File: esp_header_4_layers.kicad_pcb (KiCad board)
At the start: 4 copper layers, 27.7 x 63.5 mm, 29 parts, among them J10 BM05B-SRSS, J11 BM05B-SRSS, J12 BM05B-SRSS, J2 JST_VH_B2P, J6 BM02B-SRSS-TB, J7 B3B-EH-A, J8 B3B-EH-A, J9 B3B-EH-A, Q1 AOD472A, SW1 SW_DIP_x01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

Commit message: untracked unnecessary files
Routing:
- net /In_6V: vias 22 -> 12
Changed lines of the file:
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@@
 	(layers
 		(0 "F.Cu" signal)
-		(4 "In1.Cu" signal)
-		(6 "In2.Cu" signal)
+		(4 "In1.Cu" power "GND.Cu")
+		(6 "In2.Cu" power "POWER.Cu")
 		(2 "B.Cu" signal)
 		(9 "F.Adhes" user "F.Adhesive")
@@
 		(capping no)
 		(filling no)
+		(zone_defaults)
 		(pcbplotparams
 			(layerselection 0x00000000_00000000_55555555_5755f5ff)
@@
 	)
 	(via
-		(at 116.2 45.5)
+		(at 110 47.5)
 		(size 0.6)
 		(drill 0.3)
@@
 	)
 	(via
-		(at 114.1 45.5)
+		(at 115 42.5)
 		(size 0.6)
 		(drill 0.3)
@@
 	)
 	(via
-		(at 113.3725 50.1)
-		(size 0.6)
-		(drill 0.3)
-		(layers "F.Cu" "B.Cu")
-		(net "/In_6V")
-	)
-	(via
-		(at 112 45.5)
-		(size 0.6)
-		(drill 0.3)
-		(layers "F.Cu" "B.Cu")
-		(free yes)
-		(net "/In_6V")
-	)
-	(via
-		(at 113.4 46.2)
-		(size 0.6)
-		(drill 0.3)
-		(layers "F.Cu" "B.Cu")
-		(free yes)
-		(net "/In_6V")
-	)
-	(via
-		(at 115.5 45.5)
-		(size 0.6)
-		(drill 0.3)
-		(layers "F.Cu" "B.Cu")
-		(free yes)
-		(net "/In_6V")
-	)
-	(via
-		(at 112 46.2)
-		(size 0.6)
-		(drill 0.3)
-		(layers "F.Cu" "B.Cu")
-		(free yes)
-		(net "/In_6V")
-	)
-	(via
-		(at 112.7 45.5)
-		(size 0.6)
-		(drill 0.3)
-		(layers "F.Cu" "B.Cu")
-		(free yes)
-		(net "/In_6V")
-	)
-	(via
-		(at 111.3 46.2)
-		(size 0.6)
-		(drill 0.3)
-		(layers "F.Cu" "B.Cu")
-		(free yes)
-		(net "/In_6V")
-	)
-	(via
-		(at 114.8 46.2)
-		(size 0.6)
-		(drill 0.3)
-		(layers "F.Cu" "B.Cu")
-		(free yes)
-		(net "/In_6V")
-	)
-	(via
-		(at 116.9 46.2)
+		(at 114.846513 47.534131)
 		(size 0.6)
 		(drill 0.3)
@@
 	)
 	(via
-		(at 114.8 45.5)
+		(at 112.5 42.5)
 		(size 0.6)
 		(drill 0.3)
@@
 	)
 	(via
-		(at 116.2 46.2)
+		(at 112.5 47.5)
 		(size 0.6)
 		(drill 0.3)
@@
 	)
 	(via
-		(at 117.6 46.2)
+		(at 117.5 42.5)
 		(size 0.6)
 		(drill 0.3)
@@
 	)
 	(via
-		(at 116.9 45.5)
+		(at 110 45.1)
 		(size 0.6)
 		(drill 0.3)
@@
 	)
 	(via
-		(at 111.3 45.5)
+		(at 115 45)
 		(size 0.6)
 		(drill 0.3)
@@
 	)
 	(via
-		(at 117.6 45.5)
+		(at 112.5 45)
 		(size 0.6)
 		(drill 0.3)
@@
 	)
 	(via
-		(at 113.4 45.5)
+		(at 110 42.5)
 		(size 0.6)
 		(drill 0.3)
@@
 	)
 	(via
-		(at 115.5 46.2)
+		(at 112.5 47.5)
 		(size 0.6)
 		(drill 0.3)
@@
 	)
 	(via
-		(at 113.3725 50.1)
-		(size 0.6)
-		(drill 0.3)
-		(layers "F.Cu" "B.Cu")
-		(net "/In_6V")
-	)
-	(via
-		(at 112.7 46.2)
-		(size 0.6)
-		(drill 0.3)
-		(layers "F.Cu" "B.Cu")
-		(free yes)
-		(net "/In_6V")
-	)
-	(via
-		(at 114.1 46.2)
+		(at 117.5 47.5)
 		(size 0.6)
 		(drill 0.3)
@@
 		(start 115.6525 54.3475)
 		(end 115.6525 56.4)
-		(width 0.4)
+		(width 1)
 		(layer "F.Cu")
 		(net "+6V")
@@
 	)
 	(segment
-		(start 112.9 67.3)
-		(end 112.95 67.25)
+		(start 112.95 67.25)
+		(end 112.95 65.592648)
 		(width 0.2)
 		(layer "F.Cu")
@@
 	)
 	(segment
-		(start 112.95 67.25)
-		(end 112.95 65.592648)
+		(start 113.280647 65.262001)
+		(end 114.046 65.262001)
 		(width 0.2)
 		(layer "F.Cu")
@@
 	)
 	(segment
-		(start 112.95 65.592648)
-		(end 113.280647 65.262001)
+		(start 112.9 67.3)
+		(end 112.95 67.25)
 		(width 0.2)
 		(layer "F.Cu")
@@
 	)
 	(segment
-		(start 113.280647 65.262001)
-		(end 114.046 65.262001)
+		(start 112.95 65.592648)
+		(end 113.280647 65.262001)
 		(width 0.2)
 		(layer "F.Cu")
@@
 	)
 	(segment
-		(start 112.9 67.3)
-		(end 112.1 67.3)
+		(start 112.1 67.3)
+		(end 112.08 67.32)
 		(width 0.2)
 		(layer "B.Cu")
@@
 	)
 	(segment
-		(start 112.08 67.32)
-		(end 108.05 67.32)
+		(start 112.9 67.3)
+		(end 112.1 67.3)
 		(width 0.2)
 		(layer "B.Cu")
@@
 	)
 	(segment
-		(start 112.1 67.3)
-		(end 112.08 67.32)
+		(start 112.08 67.32)
+		(end 108.05 67.32)
 		(width 0.2)
 		(layer "B.Cu")
@@
 		(polygon
 			(pts
-				(xy 110.05139 41.519538) (xy 120.75 41.4) (xy 122.200678 42.539819) (xy 122.16867 48.435121) (xy 109.741912 48.3785)
-				(xy 109.741901 48.3785) (xy 110.051374 41.519538)
+				(xy 110 41.519538) (xy 120.75 41.4) (xy 122.200678 42.539819) (xy 122.16867 48.435121) (xy 109.741912 48.3785)
+				(xy 109.741901 48.3785) (xy 109.724906 41.52022)
 			)
 		)

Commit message: made schematic clearer
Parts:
- C2: value 10uF@12V -> 47uF@10V
- D6: value LED BLUE -> LED YELLOW
- D7: value LED Green -> LED Yellow
- Q1: value AOD472A -> MS50N06

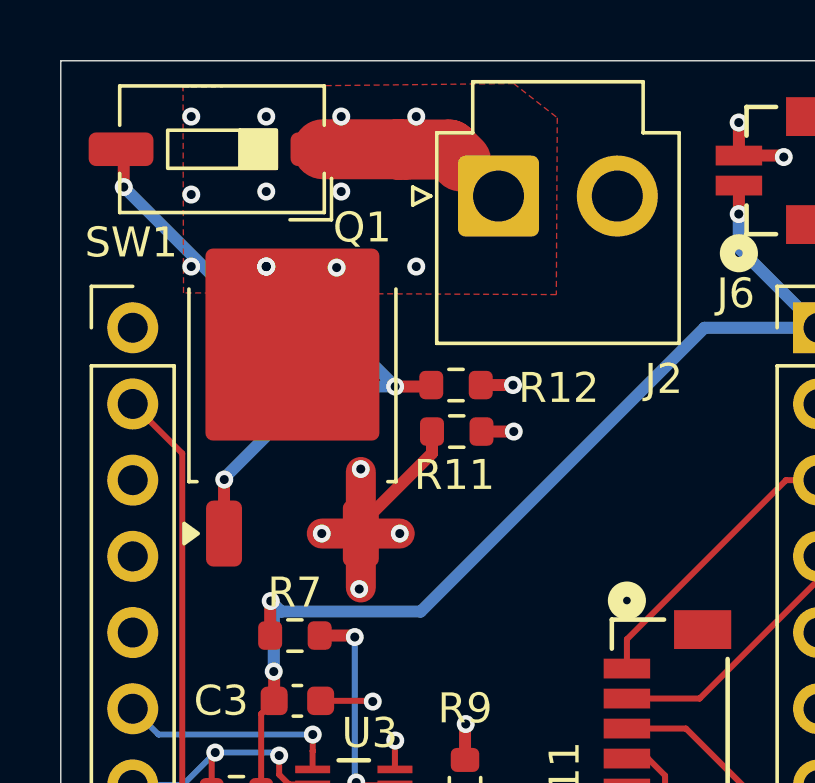
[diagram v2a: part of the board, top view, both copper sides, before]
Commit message: changed to PMOS instead of NMOS
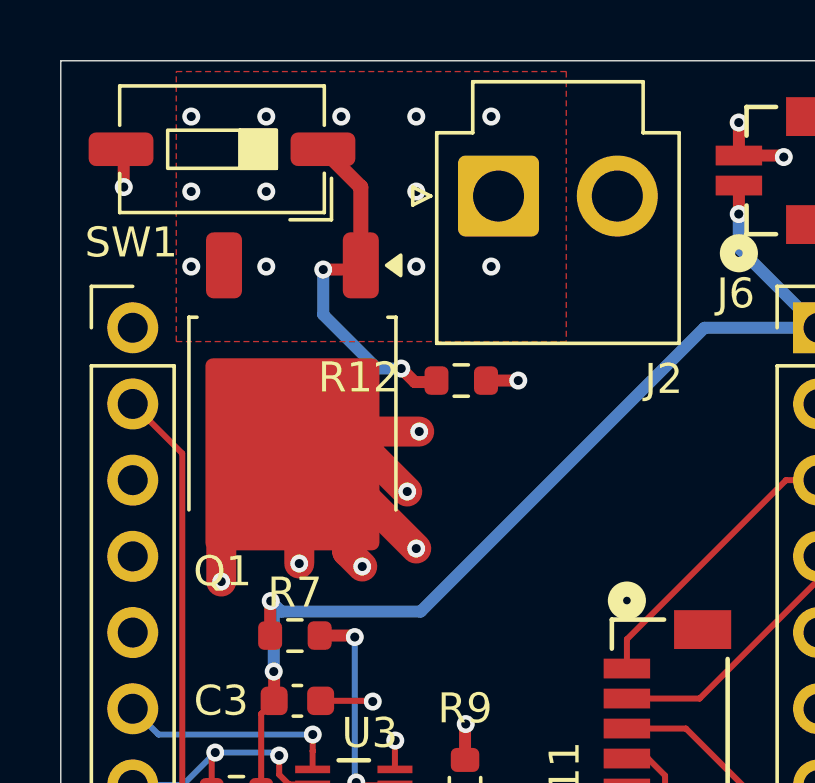
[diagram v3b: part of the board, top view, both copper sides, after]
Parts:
- removed R11: 100k, Resistor_SMD:R_0603_1608Metric
- moved Q1 1.14 mm to (113.4, 52.5), turned to -90 degrees
- moved R12 0.23 mm to (119.0, 51.3), turned to 180 degrees
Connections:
- Q1 pad D: /In_6V -> +6V
- Q1 pad S: +6V -> /In_6V
- R12 pad 1: /gate -> /In_6V
- R12 pad 2: GND -> /gate
- SW1 pad 1: /In_6V -> /gate
- SW1 pad 2: /gate -> GND
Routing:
- net +6V: track 15.2 -> 31.9 mm, vias 7 -> 9
- net /gate: track 23.0 -> 11.9 mm, vias 3 -> 2
- net /In_6V: track 4.78 -> 1.08 mm, vias 12 -> 13
- net GND: track 16.3 -> 15.4 mm, vias 13 -> 12

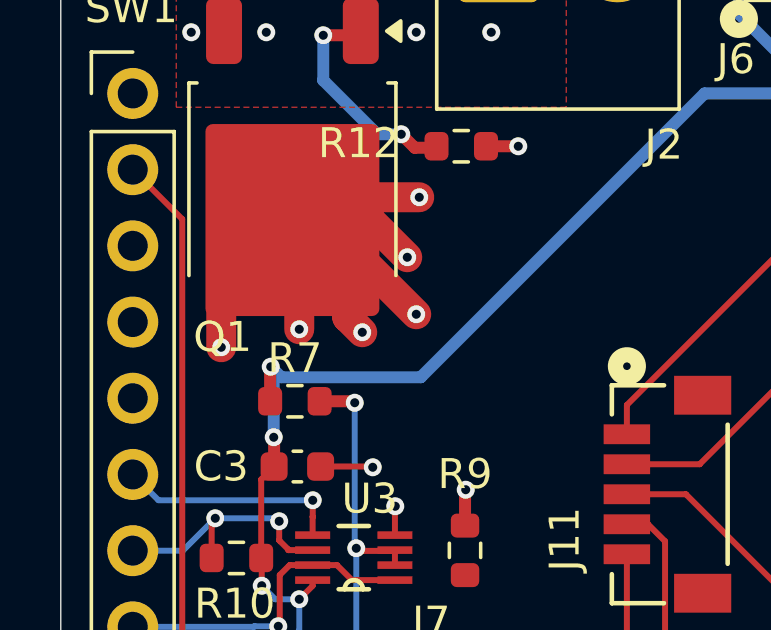
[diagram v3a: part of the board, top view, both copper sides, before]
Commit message: via size
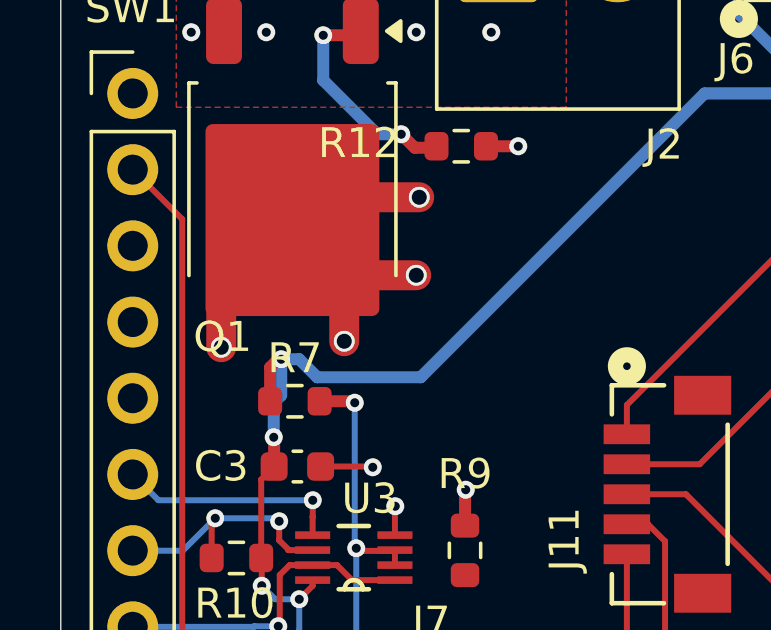
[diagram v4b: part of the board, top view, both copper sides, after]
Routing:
- net +6V: track 31.9 -> 23.3 mm, vias 9 -> 7
- net +3V3: track 80.3 -> 80.9 mm
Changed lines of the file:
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@@
-	)
-	(segment
-		(start 113.3725 55.7725)
-		(end 113.3725 53.76)
-		(width 1)
-		(layer "F.Cu")
-		(net "+6V")
 	)
 	(segment
@@
 	)
 	(segment
-		(start 115.96 53.76)
-		(end 117.2 55)
-		(width 1)
-		(layer "F.Cu")
-		(net "+6V")
-	)
-	(segment
-		(start 113.6 56)
-		(end 113.3725 55.7725)
-		(width 1)
-		(layer "F.Cu")
-		(net "+6V")
-	)
-	(segment
-		(start 115.2 57)
-		(end 115.2 55.5875)
-		(width 1)
-		(layer "F.Cu")
-		(net "+6V")
-	)
-	(segment
 		(start 113.3725 53.76)
-		(end 115.96 53.76)
-		(width 1)
-		(layer "F.Cu")
-		(net "+6V")
-	)
-	(segment
-		(start 115.7 57.5)
-		(end 115.2 57)
-		(width 1)
-		(layer "F.Cu")
-		(net "+6V")
-	)
-	(segment
-		(start 113.6 57.4)
-		(end 113.6 56)
-		(width 1)
-		(layer "F.Cu")
-		(net "+6V")
-	)
-	(segment
-		(start 115.2 55.5875)
-		(end 113.3725 53.76)
-		(width 1)
-		(layer "F.Cu")
-		(net "+6V")
-	)
-	(segment
-		(start 114.36 53.76)
-		(end 117.5 56.9)
+		(end 115.1 55.4875)
+		(width 1)
+		(layer "F.Cu")
+		(net "+6V")
+	)
+	(segment
+		(start 113.3725 53.76)
+		(end 115.2125 55.6)
+		(width 1)
+		(layer "F.Cu")
+		(net "+6V")
+	)
+	(segment
+		(start 115.1 55.4875)
+		(end 115.1 57.8)
+		(width 1)
+		(layer "F.Cu")
+		(net "+6V")
+	)
+	(segment
+		(start 115.2125 55.6)
+		(end 117.5 55.6)
 		(width 1)
 		(layer "F.Cu")
@@
 	)
 	(segment
-		(start 113.3725 53.76)
-		(end 114.36 53.76)
-		(width 1)
-		(layer "F.Cu")
-		(net "+6V")
-	)
-	(segment
 		(start 111 56.1325)
 		(end 111 58)
@@
 	(via
 		(at 111 58)
-		(size 0.6)
-		(drill 0.3)
+		(size 0.7)
+		(drill 0.5)
 		(layers "F.Cu" "B.Cu")
 		(net "+6V")
@@
 	)
 	(via
-		(at 117.2 55)
-		(size 0.6)
-		(drill 0.3)
-		(layers "F.Cu" "B.Cu")
-		(net "+6V")
-	)
-	(via
 		(at 127.85 97.95)
 		(size 0.6)
@@
 	)
 	(via
-		(at 117.5 56.9)
-		(size 0.6)
-		(drill 0.3)
+		(at 117.5 55.6)
+		(size 0.7)
+		(drill 0.5)
 		(layers "F.Cu" "B.Cu")
 		(net "+6V")
@@
 	(via
 		(at 117.6 53)
-		(size 0.6)
-		(drill 0.3)
-		(layers "F.Cu" "B.Cu")
-		(net "+6V")
-	)
-	(via
-		(at 113.6 57.4)
-		(size 0.6)
-		(drill 0.3)
-		(layers "F.Cu" "B.Cu")
-		(net "+6V")
-	)
-	(via
-		(at 115.7 57.5)
-		(size 0.6)
-		(drill 0.3)
+		(size 0.7)
+		(drill 0.5)
+		(layers "F.Cu" "B.Cu")
+		(net "+6V")
+	)
+	(via
+		(at 115.1 57.8)
+		(size 0.7)
+		(drill 0.5)
 		(layers "F.Cu" "B.Cu")
 		(net "+6V")
@@
 	)
 	(segment
+		(start 112.9 58.4)
+		(end 112.63 58.67)
+		(width 0.4)
+		(layer "F.Cu")
+		(net "+3V3")
+	)
+	(segment
 		(start 114.046 65.762002)
 		(end 114.046 65.954)
@@
 	)
 	(segment
-		(start 112.63 59.8)
-		(end 112.63 58.67)
-		(width 0.4)
-		(layer "F.Cu")
-		(net "+3V3")
-	)
-	(segment
 		(start 121.428333 97.078333)
 		(end 120.95 96.6)
@@
 	)
 	(segment
-		(start 112.63 58.67)
-		(end 112.65 58.65)
-		(width 0.4)
-		(layer "F.Cu")
-		(net "+3V3")
-	)
-	(segment
 		(start 121.428333 97.9875)
 		(end 121.428333 97.078333)
@@
 	)
 	(segment
+		(start 113 58.4)
+		(end 112.9 58.4)
+		(width 0.4)
+		(layer "F.Cu")
+		(net "+3V3")
+	)
+	(segment
+		(start 112.63 58.67)
+		(end 112.63 59.8)
+		(width 0.4)
+		(layer "F.Cu")
+		(net "+3V3")
+	)
+	(segment
 		(start 114.046 65.954)
 		(end 113.6 66.4)
@@
 	)
 	(via
-		(at 112.65 58.65)
+		(at 113 58.4)
 		(size 0.6)
 		(drill 0.3)
@@
 	)
 	(segment
+		(start 113.6 58.4)
+		(end 114.2 59)
+		(width 0.4)
+		(layer "B.Cu")
+		(net "+3V3")
+	)
+	(segment
+		(start 113 58.4)
+		(end 113 59.6)
+		(width 0.4)
+		(layer "B.Cu")
+		(net "+3V3")
+	)
+	(segment
 		(start 128.25 46.88)
 		(end 130.91 49.54)
@@
 	)
 	(segment
+		(start 127.11 49.54)
+		(end 130.91 49.54)
+		(width 0.4)
+		(layer "B.Cu")
+		(net "+3V3")
+	)
+	(segment
 		(start 120.95 96.6)
 		(end 114.5 96.6)
@@
 	)
 	(segment
-		(start 127.11 49.54)
-		(end 130.91 49.54)
-		(width 0.4)
-		(layer "B.Cu")
-		(net "+3V3")
-	)
-	(segment
 		(start 114.5 96.6)
 		(end 113.6 95.7)
@@
 	)
 	(segment
-		(start 112.65 58.65)
-		(end 113 59)
+		(start 113 58.4)
+		(end 113.6 58.4)
 		(width 0.4)
 		(layer "B.Cu")
@@
 	)
 	(segment
+		(start 117.65 59)
+		(end 127.11 49.54)
+		(width 0.4)
+		(layer "B.Cu")
+		(net "+3V3")
+	)
+	(segment
+		(start 112.75 59.85)
+		(end 112.75 61)
+		(width 0.4)
+		(layer "B.Cu")
+		(net "+3V3")
+	)
+	(segment
+		(start 113 59.6)
+		(end 112.75 59.85)
+		(width 0.4)
+		(layer "B.Cu")
+		(net "+3V3")
+	)
+	(segment
 		(start 128.25 45.75)
 		(end 128.25 46.88)
@@
 	)
 	(segment
-		(start 117.65 59)
-		(end 127.11 49.54)
-		(width 0.4)
-		(layer "B.Cu")
-		(net "+3V3")
-	)
-	(segment
-		(start 112.75 61)
-		(end 112.75 58.75)
-		(width 0.4)
-		(layer "B.Cu")
-		(net "+3V3")
-	)
-	(segment
 		(start 110.45 70.598529)
 		(end 113.6 67.448529)
@@
 	)
 	(segment
-		(start 113 59)
+		(start 114.2 59)
 		(end 117.65 59)
 		(width 0.4)
@@
 		(layer "B.Cu")
 		(net "+3V3")
-	)
-	(segment
-		(start 112.75 58.75)
-		(end 112.65 58.65)
-		(width 0.4)
-		(layer "B.Cu")
-		(net "+3V3")
